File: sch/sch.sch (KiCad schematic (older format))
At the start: 67 parts, among them P1 CONN_01X02, P10 CONN_1, P11 CONN_1, P2 CONN_02X05, P3 CONN_01X06, P4 CONN_01X06, P5 BNC, P6 Digital, P7 Analog, P8 CONN_1, P9 CONN_1, U1 PT4115, U10 DS18B20, U11 DS18B20, U12 DS18B20, U13 DS18B20, U2 PT4115, U3 PT4115, U4 PT4115, U5 PT4115, U6 PT4115, U7 LM324, U8 SALINITY_AND_LEVEL_SENSOR, U9 LM7805CT

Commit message: continued routing
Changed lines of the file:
@@
 $EndComp
 $Comp
-L GND #PWR017
+L GND #PWR016
 U 1 1 5793FDD0
 P 10900 6100
-F 0 "#PWR017" H 10900 5850 50  0001 C CNN
+F 0 "#PWR016" H 10900 5850 50  0001 C CNN
 F 1 "GND" H 10900 5950 50  0000 C CNN
 F 2 "" H 10900 6100 50  0000 C CNN
@@
 $EndComp
 $Comp
-L GND #PWR019
+L GND #PWR017
 U 1 1 579403F6
 P 5700 7100
-F 0 "#PWR019" H 5700 6850 50  0001 C CNN
+F 0 "#PWR017" H 5700 6850 50  0001 C CNN
 F 1 "GND" H 5700 6950 50  0000 C CNN
 F 2 "" H 5700 7100 50  0000 C CNN
@@
 	1    0    0    -1
 $EndComp
+Text Label 8150 2100 0    60   ~ 0
+DIM1
+Text Label 8150 2400 0    60   ~ 0
+DIM2
 Text Label 8150 1800 0    60   ~ 0
-DIM1
+DIM3
 Text Label 8150 2000 0    60   ~ 0
-DIM2
-Text Label 8150 2100 0    60   ~ 0
-DIM3
-Text Label 8150 2400 0    60   ~ 0
 DIM4
 Text Label 8150 2500 0    60   ~ 0
@@
 PH
 $Comp
-L GND #PWR020
+L GND #PWR018
 U 1 1 5794809A
 P 9000 4300
-F 0 "#PWR020" H 9000 4050 50  0001 C CNN
+F 0 "#PWR018" H 9000 4050 50  0001 C CNN
 F 1 "GND" H 9000 4150 50  0000 C CNN
 F 2 "" H 9000 4300 50  0000 C CNN
@@
 $EndComp
 $Comp
-L GND #PWR021
+L GND #PWR019
 U 1 1 57948156
 P 9600 4300
-F 0 "#PWR021" H 9600 4050 50  0001 C CNN
+F 0 "#PWR019" H 9600 4050 50  0001 C CNN
 F 1 "GND" H 9600 4150 50  0000 C CNN
 F 2 "" H 9600 4300 50  0000 C CNN
@@
 $EndComp
 $Comp
-L +5V #PWR022
+L +5V #PWR020
 U 1 1 57948735
 P 9300 4200
-F 0 "#PWR022" H 9300 4050 50  0001 C CNN
+F 0 "#PWR020" H 9300 4050 50  0001 C CNN
 F 1 "+5V" H 9300 4340 50  0000 C CNN
 F 2 "" H 9300 4200 50  0000 C CNN
@@
 $EndComp
 $Comp
-L +5V #PWR023
+L +5V #PWR021
 U 1 1 579487F8
 P 9900 4200
-F 0 "#PWR023" H 9900 4050 50  0001 C CNN
+F 0 "#PWR021" H 9900 4050 50  0001 C CNN
 F 1 "+5V" H 9900 4340 50  0000 C CNN
 F 2 "" H 9900 4200 50  0000 C CNN
@@
 T1
 $Comp
-L GND #PWR024
+L GND #PWR022
 U 1 1 579507C1
 P 7550 4450
-F 0 "#PWR024" H 7550 4200 50  0001 C CNN
+F 0 "#PWR022" H 7550 4200 50  0001 C CNN
 F 1 "GND" H 7550 4300 50  0000 C CNN
 F 2 "" H 7550 4450 50  0000 C CNN
@@
 $EndComp
 $Comp
-L +5V #PWR025
+L +5V #PWR023
 U 1 1 57950999
 P 8350 4050
-F 0 "#PWR025" H 8350 3900 50  0001 C CNN
+F 0 "#PWR023" H 8350 3900 50  0001 C CNN
 F 1 "+5V" H 8350 4190 50  0000 C CNN
 F 2 "" H 8350 4050 50  0000 C CNN
@@
 $EndComp
 $Comp
-L GND #PWR026
+L GND #PWR024
 U 1 1 57951014
 P 8000 4450
-F 0 "#PWR026" H 8000 4200 50  0001 C CNN
+F 0 "#PWR024" H 8000 4200 50  0001 C CNN
 F 1 "GND" H 8000 4300 50  0000 C CNN
 F 2 "" H 8000 4450 50  0000 C CNN
@@
 $EndComp
 $Comp
-L GND #PWR027
+L GND #PWR025
 U 1 1 5795110C
 P 8250 4450
-F 0 "#PWR027" H 8250 4200 50  0001 C CNN
+F 0 "#PWR025" H 8250 4200 50  0001 C CNN
 F 1 "GND" H 8250 4300 50  0000 C CNN
 F 2 "" H 8250 4450 50  0000 C CNN
@@
 $EndComp
 $Comp
-L GND #PWR028
+L GND #PWR026
 U 1 1 57951204
 P 7100 4450
-F 0 "#PWR028" H 7100 4200 50  0001 C CNN
+F 0 "#PWR026" H 7100 4200 50  0001 C CNN
 F 1 "GND" H 7100 4300 50  0000 C CNN
 F 2 "" H 7100 4450 50  0000 C CNN
@@
 $EndComp
 $Comp
-L GND #PWR029
+L GND #PWR027
 U 1 1 579512FC
 P 6850 4450
-F 0 "#PWR029" H 6850 4200 50  0001 C CNN
+F 0 "#PWR027" H 6850 4200 50  0001 C CNN
 F 1 "GND" H 6850 4300 50  0000 C CNN
 F 2 "" H 6850 4450 50  0000 C CNN
@@
 $EndComp
 $Comp
-L GND #PWR030
+L GND #PWR028
 U 1 1 57952AF8
 P 6150 4500
-F 0 "#PWR030" H 6150 4250 50  0001 C CNN
+F 0 "#PWR028" H 6150 4250 50  0001 C CNN
 F 1 "GND" H 6150 4350 50  0000 C CNN
 F 2 "" H 6150 4500 50  0000 C CNN
@@
 $EndComp
 $Comp
-L GND #PWR031
+L GND #PWR029
 U 1 1 5795327D
 P 4650 6400
-F 0 "#PWR031" H 4650 6150 50  0001 C CNN
+F 0 "#PWR029" H 4650 6150 50  0001 C CNN
 F 1 "GND" H 4650 6250 50  0000 C CNN
 F 2 "" H 4650 6400 50  0000 C CNN
@@
 $EndComp
 $Comp
-L GND #PWR032
+L GND #PWR030
 U 1 1 57953D90
 P 9900 5700
-F 0 "#PWR032" H 9900 5450 50  0001 C CNN
+F 0 "#PWR030" H 9900 5450 50  0001 C CNN
 F 1 "GND" H 9900 5550 50  0000 C CNN
 F 2 "" H 9900 5700 50  0000 C CNN
@@
 $EndComp
 $Comp
-L GND #PWR033
+L GND #PWR031
 U 1 1 57956710
 P 5250 6700
-F 0 "#PWR033" H 5250 6450 50  0001 C CNN
+F 0 "#PWR031" H 5250 6450 50  0001 C CNN
 F 1 "GND" H 5250 6550 50  0000 C CNN
 F 2 "" H 5250 6700 50  0000 C CNN
@@
 $EndComp
 $Comp
-L GND #PWR034
+L GND #PWR032
 U 1 1 5795681A
 P 10450 5750
-F 0 "#PWR034" H 10450 5500 50  0001 C CNN
+F 0 "#PWR032" H 10450 5500 50  0001 C CNN
 F 1 "GND" H 10450 5600 50  0000 C CNN
 F 2 "" H 10450 5750 50  0000 C CNN
@@
 $EndComp
 $Comp
-L GND #PWR036
+L GND #PWR033
 U 1 1 5795C8B8
 P 7400 6100
-F 0 "#PWR036" H 7400 5850 50  0001 C CNN
+F 0 "#PWR033" H 7400 5850 50  0001 C CNN
 F 1 "GND" H 7400 5950 50  0000 C CNN
 F 2 "" H 7400 6100 50  0000 C CNN
@@
 $EndComp
 $Comp
-L GND #PWR037
+L GND #PWR034
 U 1 1 5795C8D5
 P 6950 5700
-F 0 "#PWR037" H 6950 5450 50  0001 C CNN
+F 0 "#PWR034" H 6950 5450 50  0001 C CNN
 F 1 "GND" H 6950 5550 50  0000 C CNN
 F 2 "" H 6950 5700 50  0000 C CNN
@@
 $EndComp
 $Comp
-L GND #PWR039
+L GND #PWR035
 U 1 1 5795CD58
 P 9150 6150
-F 0 "#PWR039" H 9150 5900 50  0001 C CNN
+F 0 "#PWR035" H 9150 5900 50  0001 C CNN
 F 1 "GND" H 9150 6000 50  0000 C CNN
 F 2 "" H 9150 6150 50  0000 C CNN
@@
 $EndComp
 $Comp
-L GND #PWR040
+L GND #PWR036
 U 1 1 5795CD6F
 P 8700 5750
-F 0 "#PWR040" H 8700 5500 50  0001 C CNN
+F 0 "#PWR036" H 8700 5500 50  0001 C CNN
 F 1 "GND" H 8700 5600 50  0000 C CNN
 F 2 "" H 8700 5750 50  0000 C CNN
@@
 $EndComp
 $Comp
-L GND #PWR041
+L GND #PWR037
 U 1 1 5795D41A
 P 8150 5700
-F 0 "#PWR041" H 8150 5450 50  0001 C CNN
+F 0 "#PWR037" H 8150 5450 50  0001 C CNN
 F 1 "GND" H 8150 5550 50  0000 C CNN
 F 2 "" H 8150 5700 50  0000 C CNN
@@
 $EndComp
 $Comp
-L GND #PWR042
+L GND #PWR038
 U 1 1 5795D778
 P 6400 5650
-F 0 "#PWR042" H 6400 5400 50  0001 C CNN
+F 0 "#PWR038" H 6400 5400 50  0001 C CNN
 F 1 "GND" H 6400 5500 50  0000 C CNN
 F 2 "" H 6400 5650 50  0000 C CNN
@@
 $EndComp
 $Comp
-L GND #PWR043
+L GND #PWR039
 U 1 1 5795E7AD
 P 2850 3350
-F 0 "#PWR043" H 2850 3100 50  0001 C CNN
+F 0 "#PWR039" H 2850 3100 50  0001 C CNN
 F 1 "GND" H 2850 3200 50  0000 C CNN
 F 2 "" H 2850 3350 50  0000 C CNN
@@
 	1    0    0    -1
 $EndComp
+Text Label 2650 3050 0    60   ~ 0
+DIM1
+Text Label 3550 3050 0    60   ~ 0
+DIM2
 Text Label 2650 2950 0    60   ~ 0
-DIM1
+DIM3
 Text Label 3550 2950 0    60   ~ 0
-DIM2
-Text Label 2650 3050 0    60   ~ 0
-DIM3
-Text Label 3550 3050 0    60   ~ 0
 DIM4
 Text Label 2650 3150 0    60   ~ 0
@@
 $EndComp
 $Comp
-L GND #PWR044
+L GND #PWR040
 U 1 1 57960A2F
 P 10100 4300
-F 0 "#PWR044" H 10100 4050 50  0001 C CNN
+F 0 "#PWR040" H 10100 4050 50  0001 C CNN
 F 1 "GND" H 10100 4150 50  0000 C CNN
 F 2 "" H 10100 4300 50  0000 C CNN
@@
 $EndComp
 $Comp
-L GND #PWR045
+L GND #PWR041
 U 1 1 57960A35
 P 10700 4300
-F 0 "#PWR045" H 10700 4050 50  0001 C CNN
+F 0 "#PWR041" H 10700 4050 50  0001 C CNN
 F 1 "GND" H 10700 4150 50  0000 C CNN
 F 2 "" H 10700 4300 50  0000 C CNN
@@
 $EndComp
 $Comp
-L +5V #PWR046
+L +5V #PWR042
 U 1 1 57960A3B
 P 10400 4200
-F 0 "#PWR046" H 10400 4050 50  0001 C CNN
+F 0 "#PWR042" H 10400 4050 50  0001 C CNN
 F 1 "+5V" H 10400 4340 50  0000 C CNN
 F 2 "" H 10400 4200 50  0000 C CNN
@@
 $EndComp
 $Comp
-L +5V #PWR047
+L +5V #PWR043
 U 1 1 57960A41
 P 11000 4200
-F 0 "#PWR047" H 11000 4050 50  0001 C CNN
+F 0 "#PWR043" H 11000 4050 50  0001 C CNN
 F 1 "+5V" H 11000 4340 50  0000 C CNN
 F 2 "" H 11000 4200 50  0000 C CNN
@@
 	2950 3250 2650 3250
 $Comp
-L GND #PWR048
+L GND #PWR044
 U 1 1 579634D2
 P 3550 3350
-F 0 "#PWR048" H 3550 3100 50  0001 C CNN
+F 0 "#PWR044" H 3550 3100 50  0001 C CNN
 F 1 "GND" H 3550 3200 50  0000 C CNN
 F 2 "" H 3550 3350 50  0000 C CNN
@@
 Connection ~ 1500 1450
 $Comp
-L PWR_FLAG #FLG049
+L PWR_FLAG #FLG045
 U 1 1 57969605
 P 6200 4050
-F 0 "#FLG049" H 6200 4145 50  0001 C CNN
+F 0 "#FLG045" H 6200 4145 50  0001 C CNN
 F 1 "PWR_FLAG" H 6200 4230 50  0000 C CNN
 F 2 "" H 6200 4050 50  0000 C CNN
@@
 	900  5000 800  5000
 $Comp
-L PWR_FLAG #FLG050
+L PWR_FLAG #FLG046
 U 1 1 57957B81
 P 6150 4450
-F 0 "#FLG050" H 6150 4545 50  0001 C CNN
+F 0 "#FLG046" H 6150 4545 50  0001 C CNN
 F 1 "PWR_FLAG" H 6150 4630 50  0000 C CNN
 F 2 "" H 6150 4450 50  0000 C CNN
@@
 $EndComp
 $Comp
-L GND #PWR051
+L GND #PWR047
 U 1 1 57968DE9
 P 5750 4500
-F 0 "#PWR051" H 5750 4250 50  0001 C CNN
+F 0 "#PWR047" H 5750 4250 50  0001 C CNN
 F 1 "GND" H 5750 4350 50  0000 C CNN
 F 2 "" H 5750 4500 50  0000 C CNN
@@
 $EndComp
 $Comp
-L GND #PWR052
+L GND #PWR048
 U 1 1 5796B122
 P 2850 2450
-F 0 "#PWR052" H 2850 2200 50  0001 C CNN
+F 0 "#PWR048" H 2850 2200 50  0001 C CNN
 F 1 "GND" H 2850 2300 50  0000 C CNN
 F 2 "" H 2850 2450 50  0000 C CNN
@@
 	6750 1600 7450 1600
 $Comp
-L +BATT #PWR053
+L +BATT #PWR049
 U 1 1 57975E0D
 P 6150 4000
-F 0 "#PWR053" H 6150 3850 50  0001 C CNN
+F 0 "#PWR049" H 6150 3850 50  0001 C CNN
 F 1 "+BATT" H 6150 4140 50  0000 C CNN
 F 2 "" H 6150 4000 50  0000 C CNN
@@
 $EndComp
 $Comp
-L +BATT #PWR054
+L +BATT #PWR050
 U 1 1 57975F58
 P 6700 4050
-F 0 "#PWR054" H 6700 3900 50  0001 C CNN
+F 0 "#PWR050" H 6700 3900 50  0001 C CNN
 F 1 "+BATT" H 6700 4190 50  0000 C CNN
 F 2 "" H 6700 4050 50  0000 C CNN
@@
 	3950 6700 3450 6700
 $Comp
-L +5V #PWR?
+L +5V #PWR051
 U 1 1 579871A7
 P 5250 5950
-F 0 "#PWR?" H 5250 5800 50  0001 C CNN
+F 0 "#PWR051" H 5250 5800 50  0001 C CNN
 F 1 "+5V" H 5250 6090 50  0000 C CNN
 F 2 "" H 5250 5950 50  0000 C CNN
@@
 $EndComp
 $Comp
-L +5V #PWR?
+L +5V #PWR052
 U 1 1 57987360
 P 10450 5000
-F 0 "#PWR?" H 10450 4850 50  0001 C CNN
+F 0 "#PWR052" H 10450 4850 50  0001 C CNN
 F 1 "+5V" H 10450 5140 50  0000 C CNN
 F 2 "" H 10450 5000 50  0000 C CNN
@@
 $EndComp
 $Comp
-L +5V #PWR?
+L +5V #PWR053
 U 1 1 5798743D
 P 8700 5000
-F 0 "#PWR?" H 8700 4850 50  0001 C CNN
+F 0 "#PWR053" H 8700 4850 50  0001 C CNN
 F 1 "+5V" H 8700 5140 50  0000 C CNN
 F 2 "" H 8700 5000 50  0000 C CNN
@@
 $EndComp
 $Comp
-L +5V #PWR?
+L +5V #PWR054
 U 1 1 5798751A
 P 6950 4950
-F 0 "#PWR?" H 6950 4800 50  0001 C CNN
+F 0 "#PWR054" H 6950 4800 50  0001 C CNN
 F 1 "+5V" H 6950 5090 50  0000 C CNN
 F 2 "" H 6950 4950 50  0000 C CNN

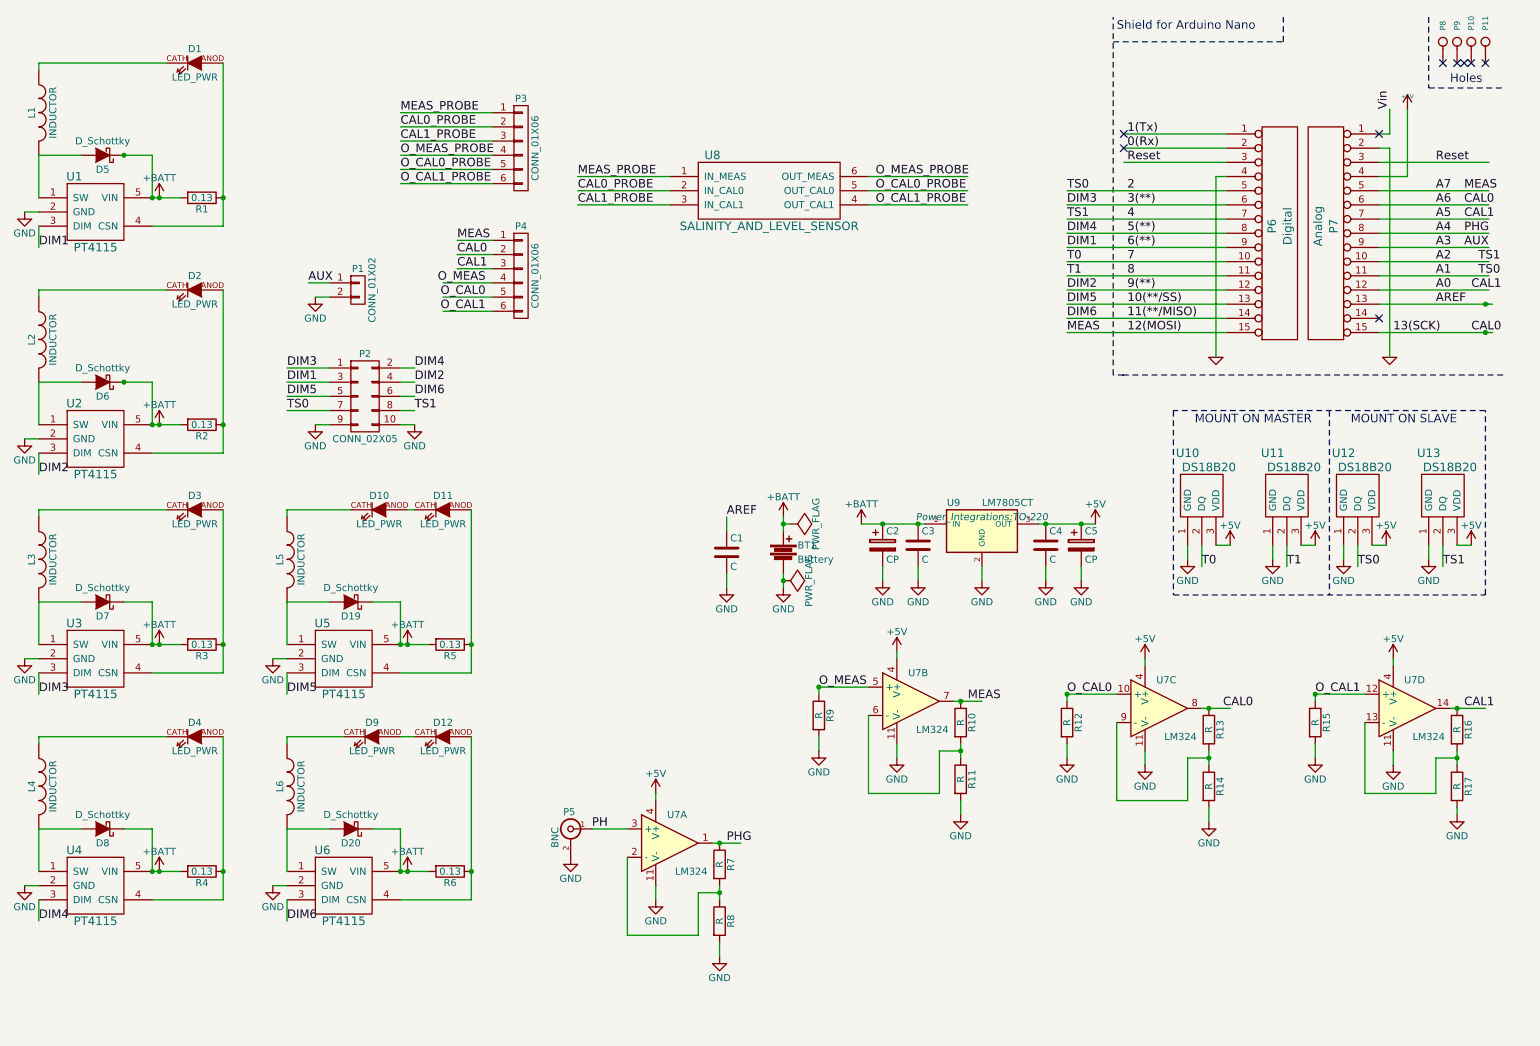
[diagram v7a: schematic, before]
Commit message: Changed some connections to make layout easier
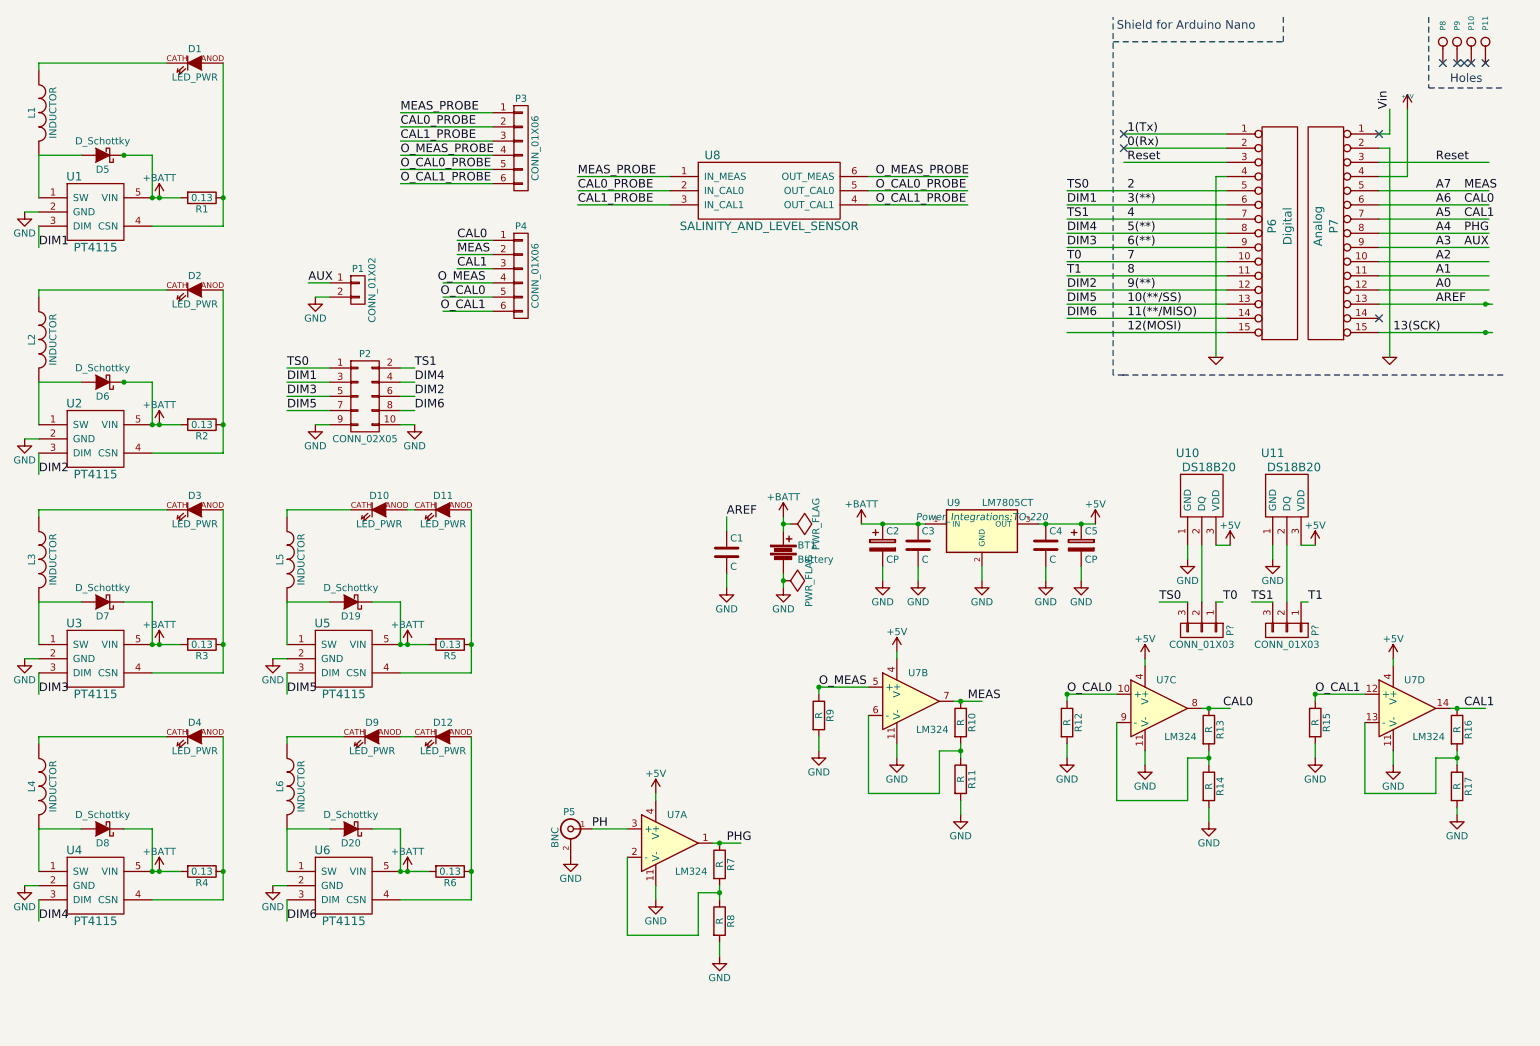
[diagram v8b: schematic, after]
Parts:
- removed U12, U13: DS18B20, TO_SOT_Packages_THT:TO-92_Inline_Narrow_Oval, symbol DS18B20
- added P? (x2): CONN_01X03, symbol CONN_01X03
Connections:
- wire segments 203 -> 201
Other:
- note removed: "MOUNT ON MASTER"
- note removed: "MOUNT ON SLAVE"
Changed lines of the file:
@@
 	1    0    0    -1
 $EndComp
-Text Label 8150 2100 0    60   ~ 0
+Text Label 8150 1800 0    60   ~ 0
 DIM1
 Text Label 8150 2400 0    60   ~ 0
 DIM2
-Text Label 8150 1800 0    60   ~ 0
+Text Label 8150 2100 0    60   ~ 0
 DIM3
 Text Label 8150 2000 0    60   ~ 0
@@
 	1    0    0    -1
 $EndComp
-Text Label 9100 4350 0    60   ~ 0
+Text Label 9250 4600 0    60   ~ 0
 T0
-Text Label 9700 4350 0    60   ~ 0
+Text Label 9850 4600 0    60   ~ 0
 T1
 Text Label 8150 2200 0    60   ~ 0
@@
 Text Label 2650 3050 0    60   ~ 0
 DIM1
+Text Label 3550 3150 0    60   ~ 0
+DIM2
+Text Label 2650 3150 0    60   ~ 0
+DIM3
 Text Label 3550 3050 0    60   ~ 0
-DIM2
-Text Label 2650 2950 0    60   ~ 0
-DIM3
-Text Label 3550 2950 0    60   ~ 0
 DIM4
-Text Label 2650 3150 0    60   ~ 0
+Text Label 2650 3250 0    60   ~ 0
 DIM5
-Text Label 3550 3150 0    60   ~ 0
+Text Label 3550 3250 0    60   ~ 0
 DIM6
 Wire Wire Line
@@
 	9300 4200 9200 4200
 Wire Wire Line
-	9100 4200 9100 4350
-Wire Wire Line
-	9700 4200 9700 4350
+	9100 4200 9100 4600
+Wire Wire Line
+	9700 4200 9700 4600
 Wire Wire Line
 	6700 4050 7150 4050
@@
 Wire Wire Line
 	3450 3050 3550 3050
-$Comp
-L DS18B20 U12
-U 1 1 57960A23
-P 10250 4150
-F 0 "U12" H 10100 4750 60  0000 C CNN
-F 1 "DS18B20" H 10250 4650 60  0000 C CNN
-F 2 "TO_SOT_Packages_THT:TO-92_Inline_Narrow_Oval" H 10250 4150 60  0001 C CNN
-F 3 "" H 10250 4150 60  0000 C CNN
-	1    10250 4150
-	1    0    0    -1
-$EndComp
-$Comp
-L DS18B20 U13
-U 1 1 57960A29
-P 10850 4150
-F 0 "U13" H 10700 4750 60  0000 C CNN
-F 1 "DS18B20" H 10850 4650 60  0000 C CNN
-F 2 "TO_SOT_Packages_THT:TO-92_Inline_Narrow_Oval" H 10850 4150 60  0001 C CNN
-F 3 "" H 10850 4150 60  0000 C CNN
-	1    10850 4150
-	1    0    0    -1
-$EndComp
-$Comp
-L GND #PWR040
-U 1 1 57960A2F
-P 10100 4300
-F 0 "#PWR040" H 10100 4050 50  0001 C CNN
-F 1 "GND" H 10100 4150 50  0000 C CNN
-F 2 "" H 10100 4300 50  0000 C CNN
-F 3 "" H 10100 4300 50  0000 C CNN
-	1    10100 4300
-	1    0    0    -1
-$EndComp
-$Comp
-L GND #PWR041
-U 1 1 57960A35
-P 10700 4300
-F 0 "#PWR041" H 10700 4050 50  0001 C CNN
-F 1 "GND" H 10700 4150 50  0000 C CNN
-F 2 "" H 10700 4300 50  0000 C CNN
-F 3 "" H 10700 4300 50  0000 C CNN
-	1    10700 4300
-	1    0    0    -1
-$EndComp
-$Comp
-L +5V #PWR042
-U 1 1 57960A3B
-P 10400 4200
-F 0 "#PWR042" H 10400 4050 50  0001 C CNN
-F 1 "+5V" H 10400 4340 50  0000 C CNN
-F 2 "" H 10400 4200 50  0000 C CNN
-F 3 "" H 10400 4200 50  0000 C CNN
-	1    10400 4200
-	1    0    0    -1
-$EndComp
-$Comp
-L +5V #PWR043
-U 1 1 57960A41
-P 11000 4200
-F 0 "#PWR043" H 11000 4050 50  0001 C CNN
-F 1 "+5V" H 11000 4340 50  0000 C CNN
-F 2 "" H 11000 4200 50  0000 C CNN
-F 3 "" H 11000 4200 50  0000 C CNN
-	1    11000 4200
-	1    0    0    -1
-$EndComp
-Text Label 10200 4350 0    60   ~ 0
+Text Label 8800 4600 0    60   ~ 0
 TS0
-Text Label 10800 4350 0    60   ~ 0
+Text Label 9450 4600 0    60   ~ 0
 TS1
-Wire Wire Line
-	10700 4200 10700 4300
-Wire Wire Line
-	10100 4200 10100 4300
-Wire Wire Line
-	11000 4200 10900 4200
-Wire Wire Line
-	10400 4200 10300 4200
-Wire Wire Line
-	10200 4200 10200 4350
-Wire Wire Line
-	10800 4200 10800 4350
-Text Label 2650 3250 0    60   ~ 0
+Text Label 2650 2950 0    60   ~ 0
 TS0
-Text Label 3550 3250 0    60   ~ 0
+Text Label 3550 2950 0    60   ~ 0
 TS1
 Text Label 5750 6300 0    60   ~ 0
@@
 Wire Wire Line
 	3550 3350 3450 3350
-Wire Notes Line
-	10000 3250 10000 4550
-Wire Notes Line
-	8900 4550 11100 4550
-Wire Notes Line
-	11100 4550 11100 3250
-Wire Notes Line
-	11100 3250 8900 3250
-Wire Notes Line
-	8900 3250 8900 4550
-Text Notes 9050 3350 0    60   ~ 0
-MOUNT ON MASTER
-Text Notes 10150 3350 0    60   ~ 0
-MOUNT ON SLAVE
 $Comp
 L Battery BT1
@@
 Wire Wire Line
 	4100 2250 3850 2250
+Text Label 3850 2150 0    60   ~ 0
+MEAS
 Text Label 3850 2050 0    60   ~ 0
-MEAS
-Text Label 3850 2150 0    60   ~ 0
 CAL0
 Text Label 3850 2250 0    60   ~ 0
-CAL1
-Text Label 8150 2700 0    60   ~ 0
-MEAS
-Text Label 11000 2700 0    60   ~ 0
-CAL0
-Text Label 11000 2400 0    60   ~ 0
 CAL1
 $Comp
@@
 Text Label 10950 2000 0    60   ~ 0
 PHG
-Text Label 11050 2300 0    60   ~ 0
-TS0
-Text Label 11050 2200 0    60   ~ 0
-TS1
 $Comp
 L CONN_01X02 P1
@@
 	1    0    0    -1
 $EndComp
+$Comp
+L CONN_01X03 P?
+U 1 1 57B3E354
+P 9100 4800
+F 0 "P?" H 9100 5000 50  0000 C CNN
+F 1 "CONN_01X03" V 9200 4800 50  0000 C CNN
+F 2 "" H 9100 4800 50  0000 C CNN
+F 3 "" H 9100 4800 50  0000 C CNN
+	1    9100 4800
+	0    1    1    0
+$EndComp
+$Comp
+L CONN_01X03 P?
+U 1 1 57B3E4BD
+P 9700 4800
+F 0 "P?" H 9700 5000 50  0000 C CNN
+F 1 "CONN_01X03" V 9800 4800 50  0000 C CNN
+F 2 "" H 9700 4800 50  0000 C CNN
+F 3 "" H 9700 4800 50  0000 C CNN
+	1    9700 4800
+	0    1    1    0
+$EndComp
+Wire Wire Line
+	9800 4600 9850 4600
+Wire Wire Line
+	9600 4600 9450 4600
+Wire Wire Line
+	9200 4600 9250 4600
+Wire Wire Line
+	9000 4600 8800 4600
 $EndSCHEMATC
